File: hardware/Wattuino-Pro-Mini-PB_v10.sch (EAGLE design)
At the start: 26 parts, among them IC1A ATMEGA328PB-AU, IC1B ATMEGA328PB-MU, IC2 VREG-TS9011-5V, Q1 16MHz, X1 PASSER-07, X2 PASSER-07, X3 PASSER-07

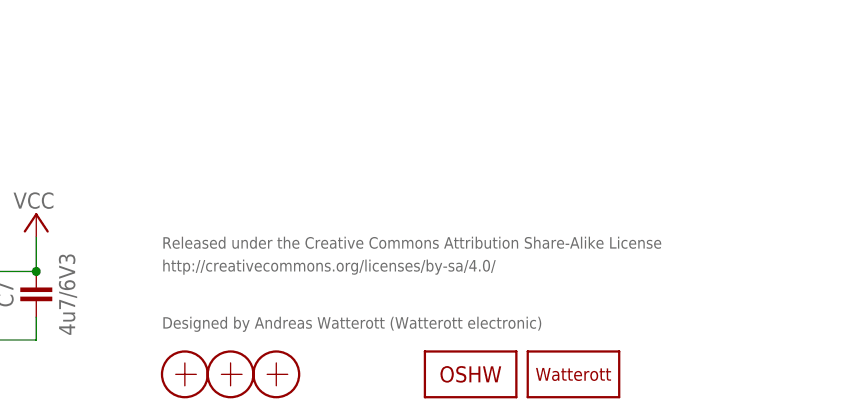
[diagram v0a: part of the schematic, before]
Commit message: updated schematics
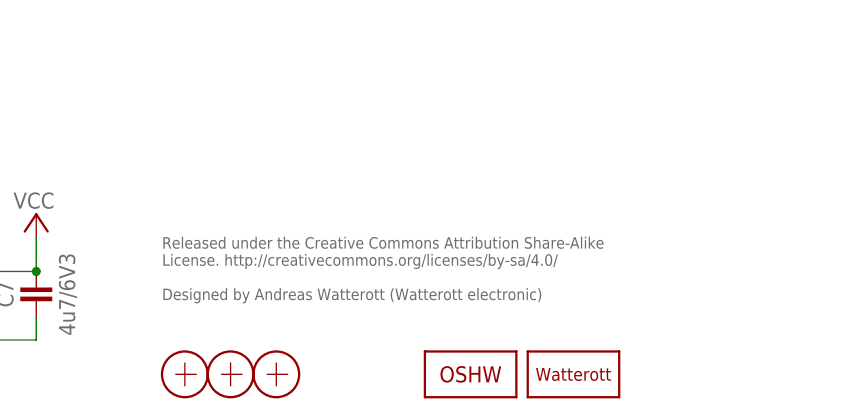
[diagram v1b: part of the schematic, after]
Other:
- note added: "Released under the Creative Commons Attribution Share-Alike License. http://creativecommons.org/licenses/by-sa/4.0/ Designed by Andreas Watterott (Watterott electronic)"
- note removed: "Designed by Andreas Watterott (Watterott electronic)"
- note removed: "Released under the Creative Commons Attribution Share-Alike License"
- note removed: "http://creativecommons.org/licenses/by-sa/4.0/"
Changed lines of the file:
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@@
 <layer number="51" name="tDocu" color="7" fill="1" visible="no" active="no"/>
 <layer number="52" name="bDocu" color="7" fill="1" visible="no" active="no"/>
-<layer number="53" name="tGND_GNDA" color="7" fill="9" visible="no" active="no"/>
-<layer number="54" name="bGND_GNDA" color="1" fill="9" visible="no" active="no"/>
-<layer number="56" name="wert" color="7" fill="1" visible="no" active="no"/>
 <layer number="90" name="Modules" color="5" fill="1" visible="yes" active="yes"/>
 <layer number="91" name="Nets" color="2" fill="1" visible="yes" active="yes"/>
@@
 <layer number="98" name="Guide" color="6" fill="1" visible="yes" active="yes"/>
 <layer number="99" name="SpiceOrder" color="5" fill="1" visible="yes" active="yes"/>
-<layer number="100" name="Muster" color="7" fill="1" visible="no" active="no"/>
-<layer number="101" name="Patch_Top" color="12" fill="4" visible="no" active="yes"/>
-<layer number="102" name="Vscore" color="7" fill="1" visible="no" active="yes"/>
-<layer number="103" name="tMap" color="7" fill="1" visible="no" active="yes"/>
-<layer number="104" name="Name" color="16" fill="1" visible="no" active="yes"/>
-<layer number="105" name="tPlate" color="7" fill="1" visible="no" active="yes"/>
-<layer number="106" name="bPlate" color="7" fill="1" visible="no" active="yes"/>
-<layer number="107" name="Crop" color="7" fill="1" visible="no" active="yes"/>
-<layer number="116" name="Patch_BOT" color="9" fill="4" visible="no" active="yes"/>
-<layer number="121" name="_tsilk" color="7" fill="1" visible="no" active="yes"/>
-<layer number="122" name="_bsilk" color="7" fill="1" visible="no" active="yes"/>
-<layer number="125" name="_tNames" color="7" fill="1" visible="no" active="yes"/>
-<layer number="144" name="Drill_legend" color="7" fill="1" visible="no" active="yes"/>
-<layer number="151" name="HeatSink" color="7" fill="1" visible="no" active="yes"/>
-<layer number="200" name="200bmp" color="1" fill="10" visible="no" active="yes"/>
-<layer number="201" name="201bmp" color="2" fill="10" visible="no" active="yes"/>
-<layer number="202" name="202bmp" color="3" fill="10" visible="no" active="yes"/>
-<layer number="203" name="203bmp" color="4" fill="10" visible="no" active="yes"/>
-<layer number="204" name="204bmp" color="5" fill="10" visible="no" active="yes"/>
-<layer number="205" name="205bmp" color="6" fill="10" visible="no" active="yes"/>
-<layer number="206" name="206bmp" color="7" fill="10" visible="no" active="yes"/>
-<layer number="207" name="207bmp" color="8" fill="10" visible="no" active="yes"/>
-<layer number="208" name="208bmp" color="9" fill="10" visible="no" active="yes"/>
-<layer number="209" name="209bmp" color="7" fill="1" visible="no" active="yes"/>
-<layer number="210" name="210bmp" color="7" fill="1" visible="no" active="yes"/>
-<layer number="211" name="211bmp" color="7" fill="1" visible="no" active="yes"/>
-<layer number="212" name="212bmp" color="7" fill="1" visible="no" active="yes"/>
-<layer number="213" name="213bmp" color="7" fill="1" visible="no" active="yes"/>
-<layer number="214" name="214bmp" color="7" fill="1" visible="no" active="yes"/>
-<layer number="215" name="215bmp" color="7" fill="1" visible="no" active="yes"/>
-<layer number="216" name="216bmp" color="7" fill="1" visible="no" active="yes"/>
-<layer number="217" name="217bmp" color="18" fill="1" visible="no" active="no"/>
-<layer number="218" name="218bmp" color="19" fill="1" visible="no" active="no"/>
-<layer number="219" name="219bmp" color="20" fill="1" visible="no" active="no"/>
-<layer number="220" name="220bmp" color="21" fill="1" visible="no" active="no"/>
-<layer number="221" name="221bmp" color="22" fill="1" visible="no" active="no"/>
-<layer number="222" name="222bmp" color="23" fill="1" visible="no" active="no"/>
-<layer number="223" name="223bmp" color="24" fill="1" visible="no" active="no"/>
-<layer number="224" name="224bmp" color="25" fill="1" visible="no" active="no"/>
-<layer number="250" name="Descript" color="3" fill="1" visible="no" active="no"/>
-<layer number="251" name="SMDround" color="12" fill="11" visible="no" active="no"/>
-<layer number="254" name="cooling" color="7" fill="1" visible="no" active="yes"/>
 </layers>
 <schematic xreflabel="%F%N/%S.%C%R" xrefpart="/%S.%C%R">
@@
 <sheet>
 <plain>
-<text x="162.56" y="21.59" size="1.27" layer="95">Released under the Creative Commons Attribution Share-Alike License</text>
-<text x="162.56" y="19.05" size="1.27" layer="95">http://creativecommons.org/licenses/by-sa/4.0/</text>
-<text x="162.56" y="12.7" size="1.27" layer="95">Designed by Andreas Watterott (Watterott electronic)</text>
+<text x="162.56" y="22.86" size="1.27" layer="95" align="top-left">Released under the Creative Commons Attribution Share-Alike
+License. http://creativecommons.org/licenses/by-sa/4.0/
+Designed by Andreas Watterott (Watterott electronic)</text>
 </plain>
 <instances>
@@
 </schematic>
 </drawing>
+<compatibility>
+<note version="6.3" minversion="6.2.2" severity="warning">
+Since Version 6.2.2 text objects can contain more than one line,
+which will not be processed correctly with this version.
+</note>
+</compatibility>
 </eagle>
